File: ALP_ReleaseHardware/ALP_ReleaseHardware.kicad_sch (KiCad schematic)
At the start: 0 parts

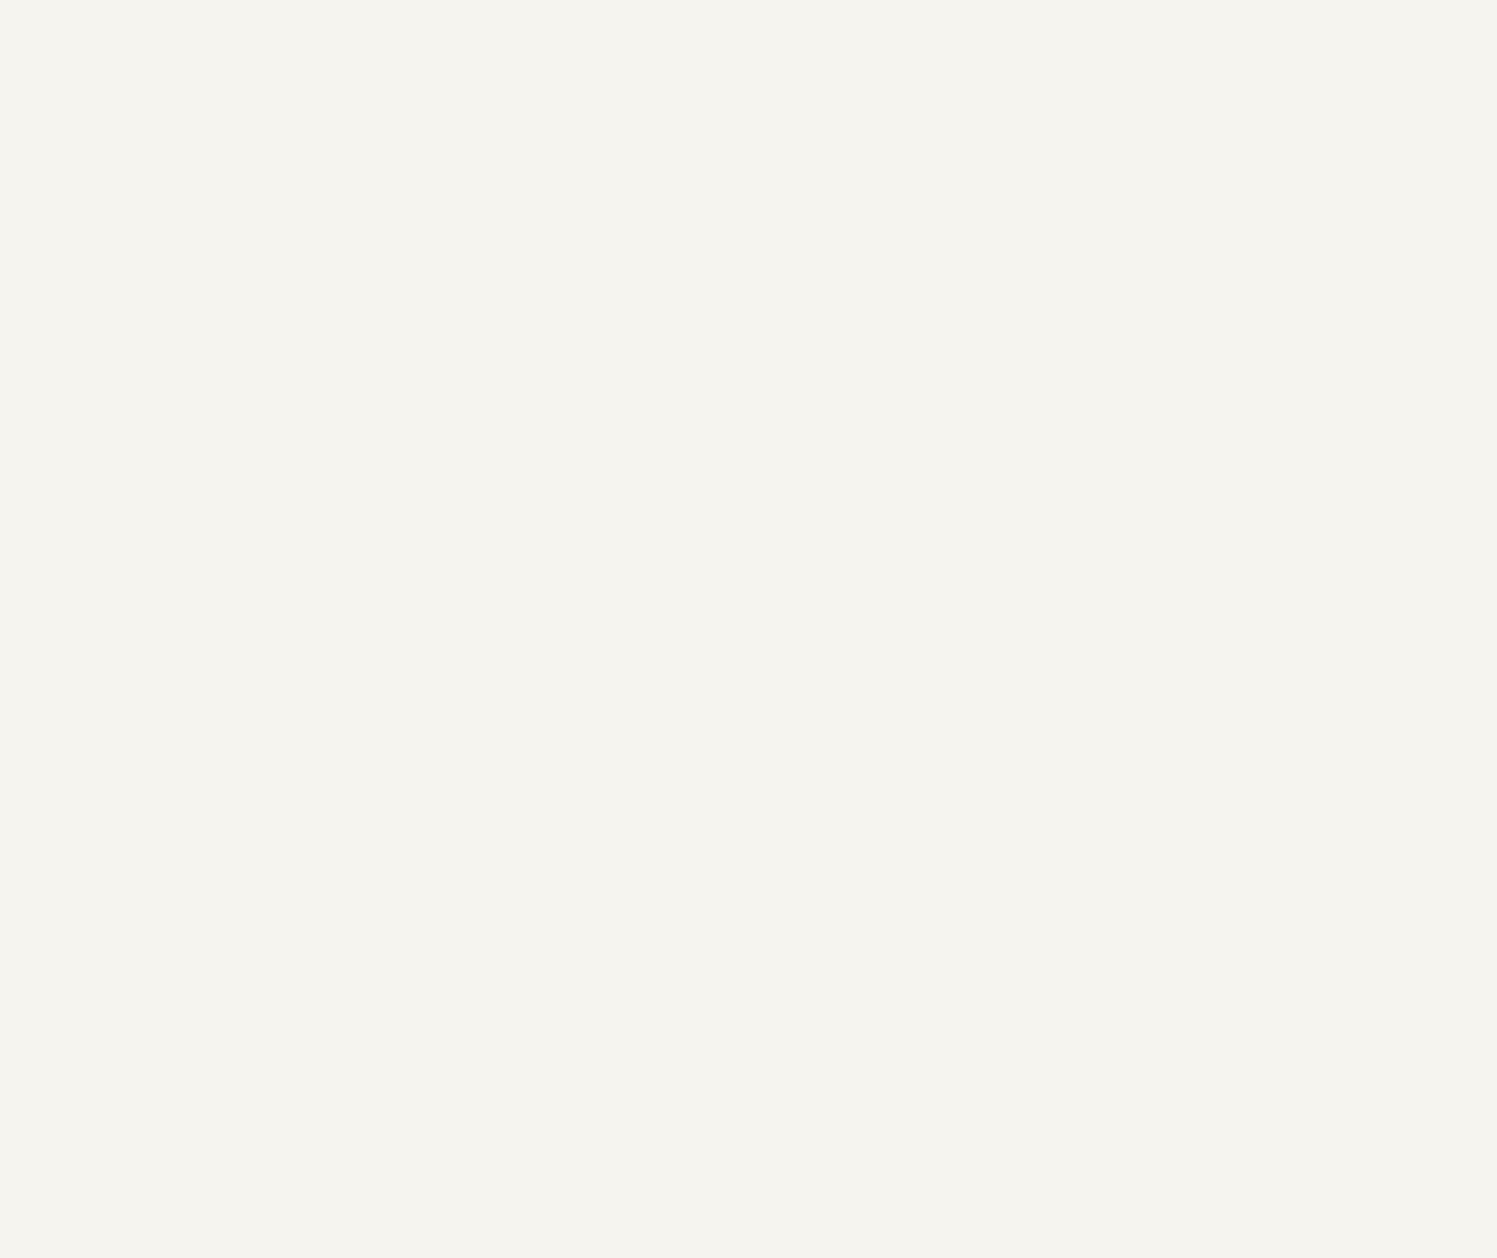
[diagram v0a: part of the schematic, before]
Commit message: ATMEGA32U4 selected
Power circuitry completed
Analog power circuitry completed
External crystal circuitry completed
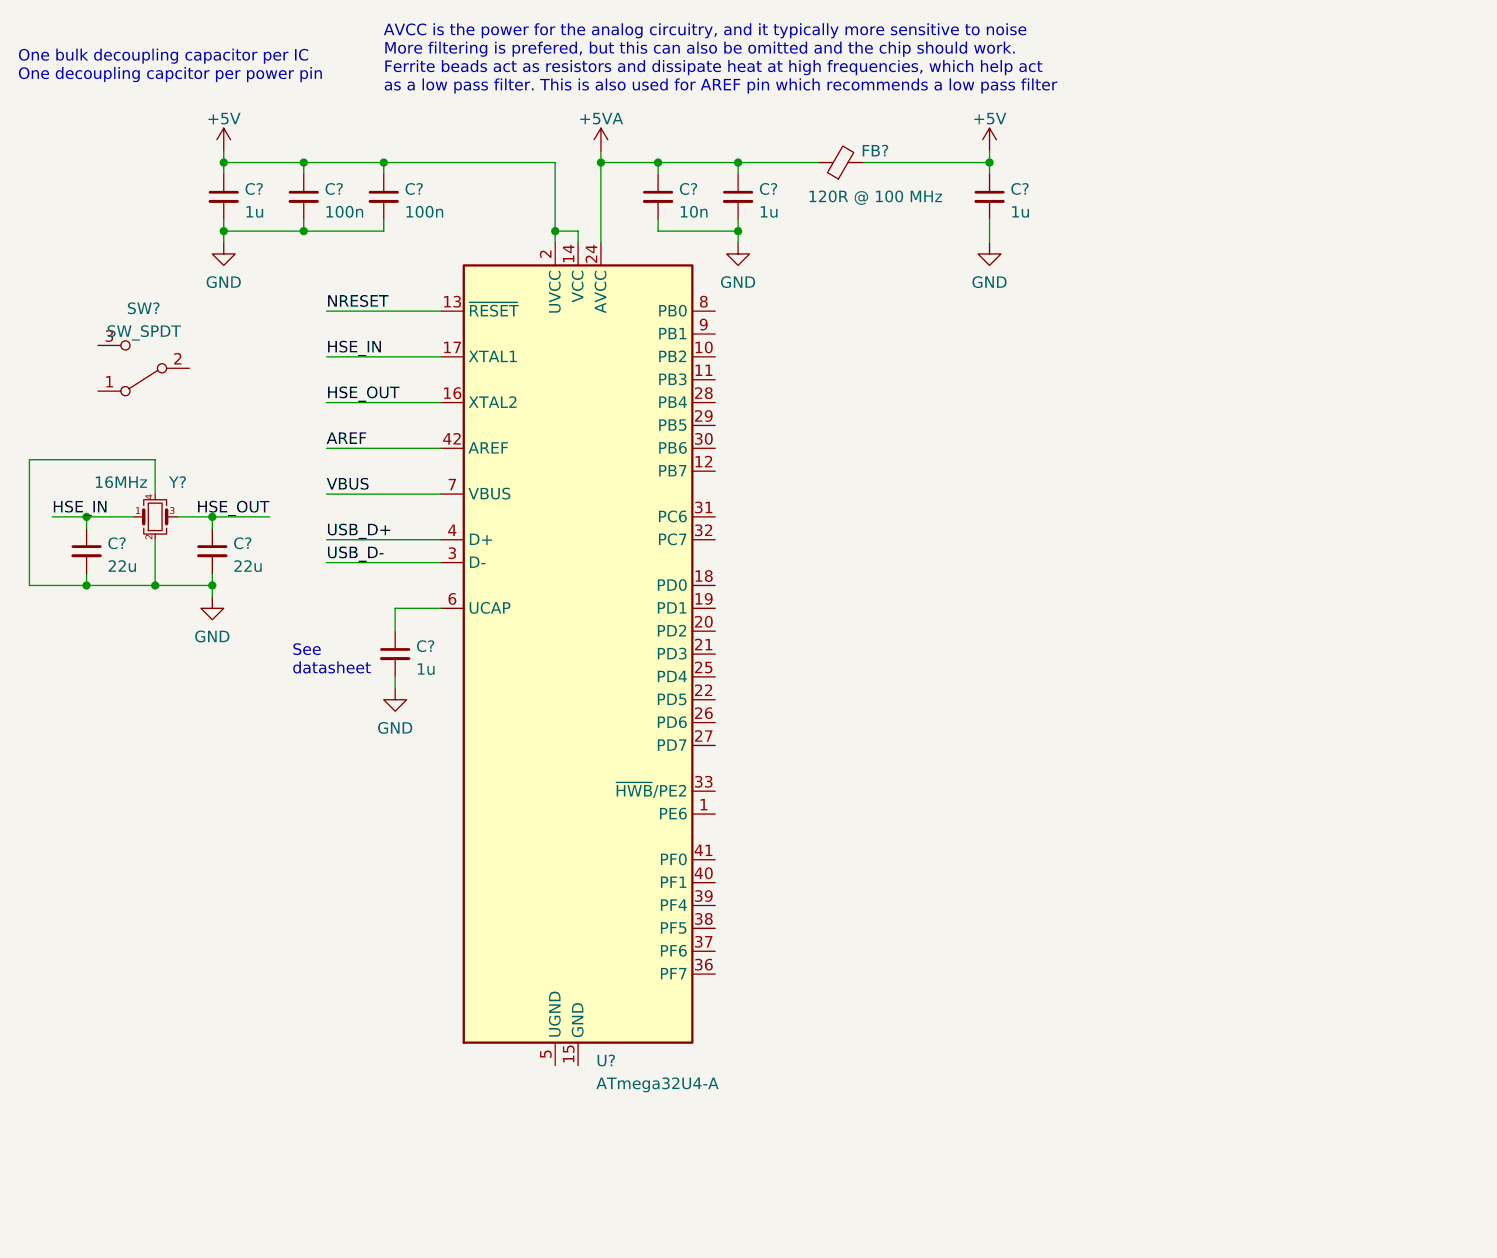
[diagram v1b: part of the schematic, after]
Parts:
- added C? (x4): 1u, symbol Device:C_Small
- added C? (x2): 100n, symbol Device:C_Small
- added C?: 10n, symbol Device:C_Small
- added C? (x2): 22u, symbol Device:C_Small
- added FB?: 120R @ 100 MHz, symbol Device:FerriteBead_Small
- added SW?: SW_SPDT, symbol Switch:SW_SPDT
- added U?: ATmega32U4-A, Package_QFP:TQFP-44_10x10mm_P0.8mm, symbol MCU_Microchip_ATmega:ATmega32U4-A
- added Y?: 16MHz, symbol Device:Crystal_GND24_Small
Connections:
- new net: C?.1, U?.6 (UCAP)
- new net: U?.15 (GND), U?.23 (GND), U?.35 (GND), U?.43 (GND)
- new net +5V: C?.1, C?.1, C?.1, C?.1, FB?.2, U?.14 (VCC), U?.2 (UVCC), U?.34 (VCC)
- new net +5VA: C?.1, C?.1, FB?.1, U?.24 (AVCC), U?.44 (AVCC)
- new net AREF: U?.42 (AREF)
- new net GND: C?.2, C?.2, C?.2, C?.2, C?.2, C?.2, C?.2, C?.2, C?.2, Y?.2, Y?.4
- new net HSE_IN: C?.1, U?.17 (XTAL1), Y?.1
- new net HSE_OUT: C?.1, U?.16 (XTAL2), Y?.3
- new net NRESET: U?.13 (~{RESET})
- new net USB_D+: U?.4 (D+)
- new net USB_D-: U?.3 (D-)
- new net VBUS: U?.7 (VBUS)
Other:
- note added: "AVCC is the power for the analog circuitry, and it typically more sensitive to noise More filtering is prefered, but this can also be omitted and the chip should work. Ferrite beads act as resistors and dissipate heat at high frequencies, which help act as a low pass filter. This is also used for AREF pin which recommends a low pass filter"
- note added: "One bulk decoupling capacitor per IC One decoupling capcitor per power pin"
- note added: "See datasheet"

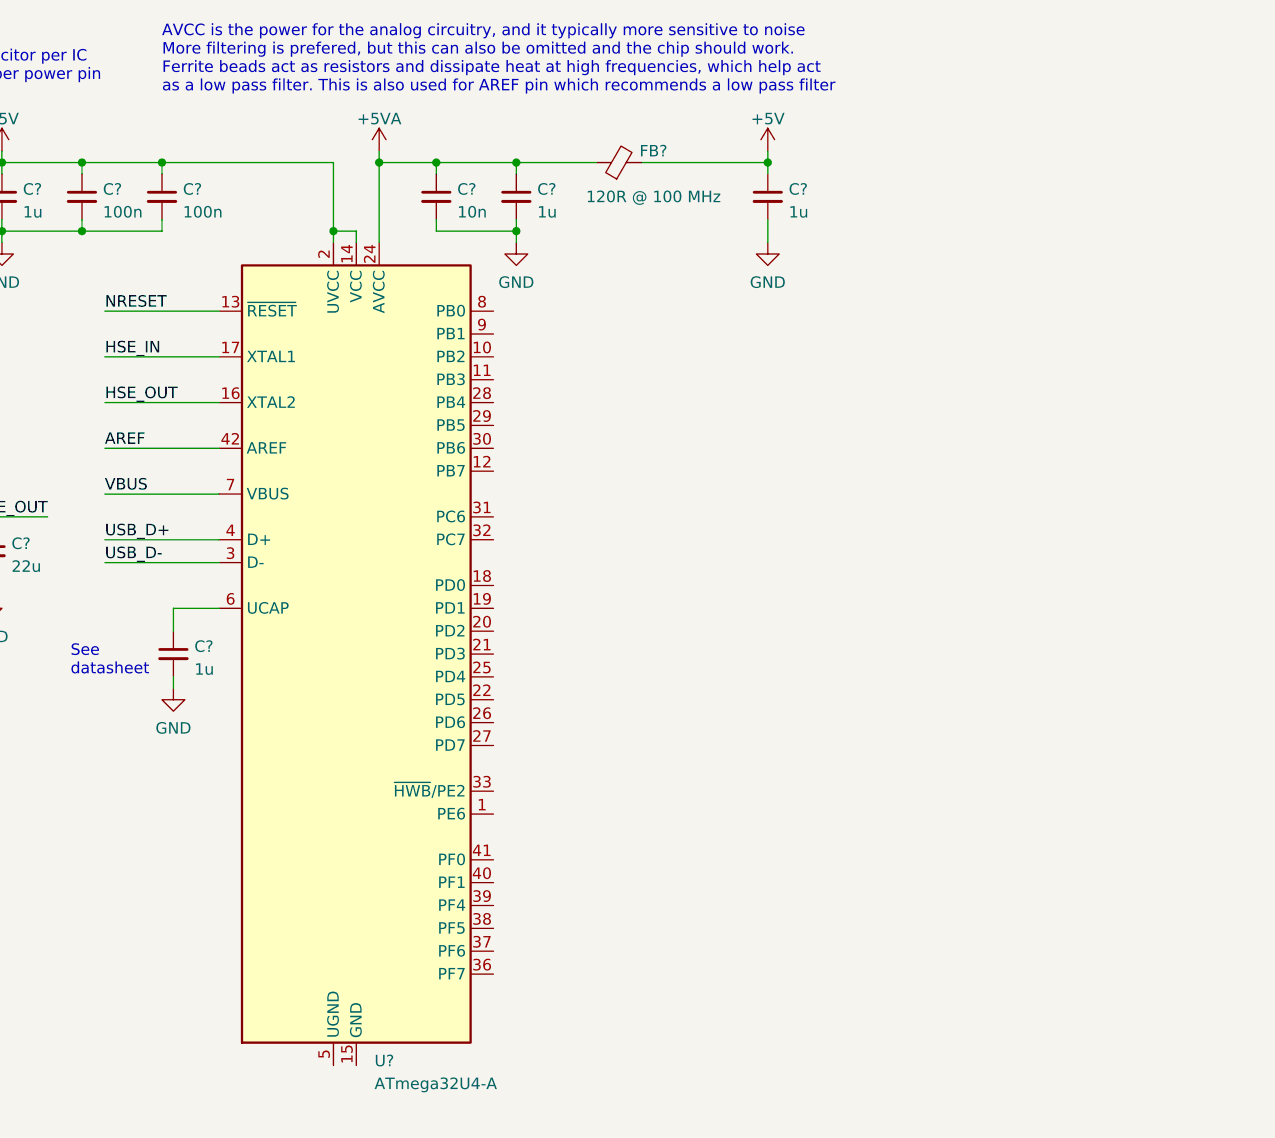
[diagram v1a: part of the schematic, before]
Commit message: Arduino micro pinouts added
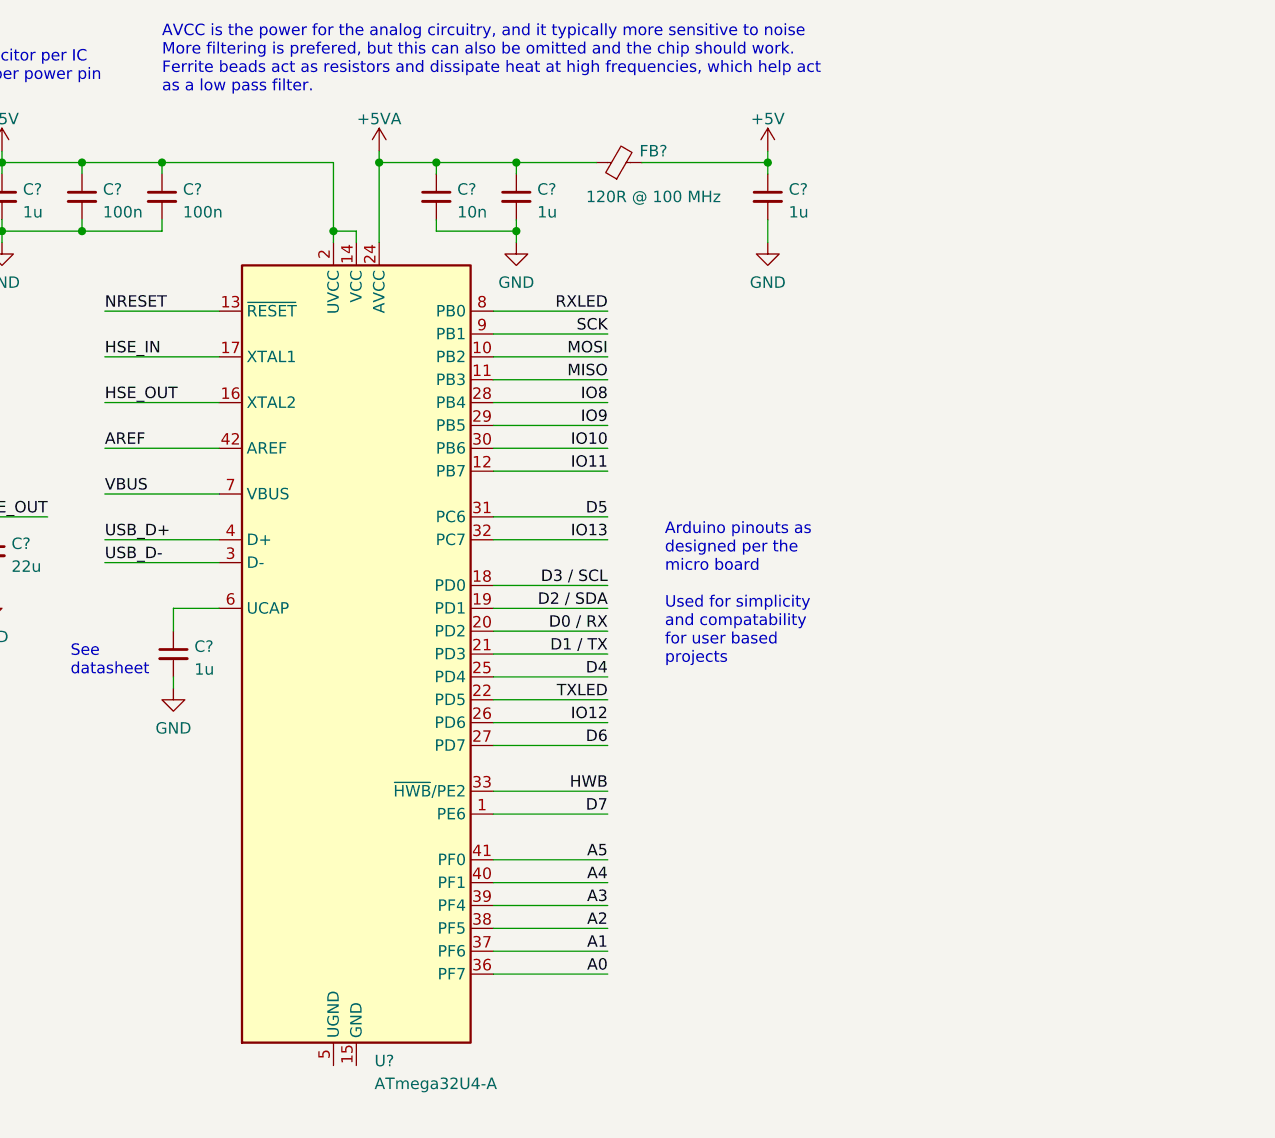
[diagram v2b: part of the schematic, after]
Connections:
- net D7: now reaches U?.1 (PE6)
- net MOSI: now reaches U?.10 (PB2)
- net MISO: now reaches U?.11 (PB3)
- net IO11: now reaches U?.12 (PB7)
- net D3 / SCL: now reaches U?.18 (PD0)
- net D2 / SDA: now reaches U?.19 (PD1)
- net D0 / RX: now reaches U?.20 (PD2)
- net D1 / TX: now reaches U?.21 (PD3)
- net TXLED: now reaches U?.22 (PD5)
- net D4: now reaches U?.25 (PD4)
- net IO12: now reaches U?.26 (PD6)
- net D6: now reaches U?.27 (PD7)
- net IO8: now reaches U?.28 (PB4)
- net IO9: now reaches U?.29 (PB5)
- net IO10: now reaches U?.30 (PB6)
- net D5: now reaches U?.31 (PC6)
- net IO13: now reaches U?.32 (PC7)
- net HWB: now reaches U?.33 (~{HWB}/PE2)
- net A0: now reaches U?.36 (PF7)
- net A1: now reaches U?.37 (PF6)
- net A2: now reaches U?.38 (PF5)
- net A3: now reaches U?.39 (PF4)
- net A4: now reaches U?.40 (PF1)
- net A5: now reaches U?.41 (PF0)
- net RXLED: now reaches U?.8 (PB0)
- net SCK: now reaches U?.9 (PB1)
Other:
- note added: "AVCC is the power for the analog circuitry, and it typically more sensitive to noise More filtering is prefered, but this can also be omitted and the chip should work. Ferrite beads act as resistors and dissipate heat at high frequencies, which help act as a low pass filter."
- note added: "Arduino pinouts as designed per the micro board Used for simplicity and compatability for user based projects"
- note removed: "AVCC is the power for the analog circuitry, and it typically more sensitive to noise More filtering is prefered, but this can also be omitted and the chip should work. Ferrite beads act as resistors and dissipate heat at high frequencies, which help act as a low pass filter. This is also used for AREF pin which recommends a low pass filter"
